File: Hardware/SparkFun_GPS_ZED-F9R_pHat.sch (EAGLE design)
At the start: 87 parts, among them J1 U.FL, J5 QWIIC_RIGHT_ANGLE, J6 RASPBERRYPI-40-PIN-GPIO_SMD_S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, U1 UBLOX_ZED_F9R, U2 HCPL-073L, U3 UHS_INVERTER_SCHMITT_TRIGGERS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, U4 UHS_INVERTER_SCHMITT_TRIGGERS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

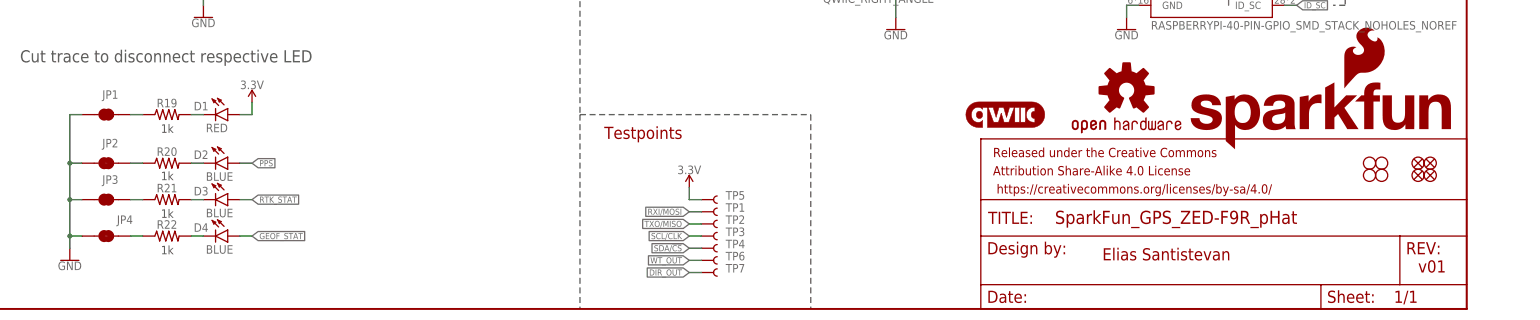
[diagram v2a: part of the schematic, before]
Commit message: Fixe RF trace, fixes silk, moves version number, fixes D+ and D- traces
* Changes jumper labels in schematic
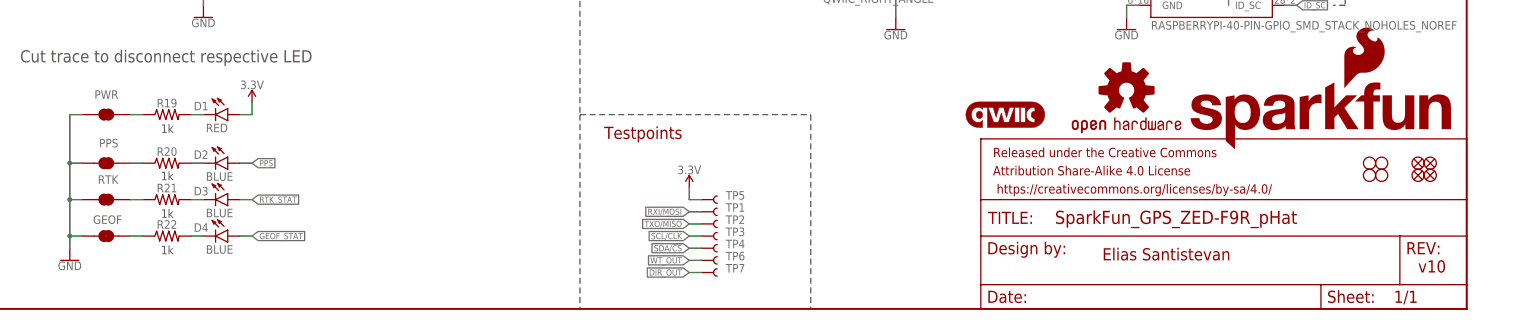
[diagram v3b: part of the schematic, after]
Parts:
- renumbered JP1 to PWR, JP2 to PPS, JP3 to RTK, JP4 to GEOF
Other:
- note added: "v10"
- note removed: "v01"
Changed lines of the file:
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@@
 <part name="R19" library="SparkFun-Resistors" deviceset="1KOHM" device="-0603-1/10W-1%" value="1k"/>
 <part name="SUPPLY7" library="SparkFun-PowerSymbols" deviceset="3.3V" device=""/>
-<part name="JP1" library="SparkFun-Jumpers" deviceset="JUMPER-SMT_2_NC_TRACE" device="_SILK" package3d_urn="urn:adsk.eagle:package:39281/1" value="JUMPER-SMT_2_NC_TRACE_SILK"/>
+<part name="PWR" library="SparkFun-Jumpers" deviceset="JUMPER-SMT_2_NC_TRACE" device="_SILK" package3d_urn="urn:adsk.eagle:package:39281/1" value="JUMPER-SMT_2_NC_TRACE_SILK"/>
 <part name="GND6" library="SparkFun-PowerSymbols" deviceset="GND" device=""/>
 <part name="GND7" library="SparkFun-PowerSymbols" deviceset="GND" device=""/>
@@
 <part name="R20" library="SparkFun-Resistors" deviceset="1KOHM" device="-0603-1/10W-1%" value="1k"/>
 <part name="R21" library="SparkFun-Resistors" deviceset="1KOHM" device="-0603-1/10W-1%" value="1k"/>
-<part name="JP3" library="SparkFun-Jumpers" deviceset="JUMPER-SMT_2_NC_TRACE" device="_SILK" package3d_urn="urn:adsk.eagle:package:39281/1" value="JUMPER-SMT_2_NC_TRACE_SILK"/>
-<part name="JP2" library="SparkFun-Jumpers" deviceset="JUMPER-SMT_2_NC_TRACE" device="_SILK" package3d_urn="urn:adsk.eagle:package:39281/1" value="JUMPER-SMT_2_NC_TRACE_SILK"/>
+<part name="RTK" library="SparkFun-Jumpers" deviceset="JUMPER-SMT_2_NC_TRACE" device="_SILK" package3d_urn="urn:adsk.eagle:package:39281/1" value="JUMPER-SMT_2_NC_TRACE_SILK"/>
+<part name="PPS" library="SparkFun-Jumpers" deviceset="JUMPER-SMT_2_NC_TRACE" device="_SILK" package3d_urn="urn:adsk.eagle:package:39281/1" value="JUMPER-SMT_2_NC_TRACE_SILK"/>
 <part name="GND19" library="SparkFun-PowerSymbols" deviceset="GND" device=""/>
 <part name="D2" library="SparkFun-LED" deviceset="LED-BLUE" device="0603" value="BLUE"/>
@@
 <part name="GND9" library="SparkFun-PowerSymbols" deviceset="GND" device=""/>
 <part name="R22" library="SparkFun-Resistors" deviceset="1KOHM" device="-0603-1/10W-1%" value="1k"/>
-<part name="JP4" library="SparkFun-Jumpers" deviceset="JUMPER-SMT_2_NC_TRACE" device="_SILK" package3d_urn="urn:adsk.eagle:package:39281/1" value="JUMPER-SMT_2_NC_TRACE_SILK"/>
+<part name="GEOF" library="SparkFun-Jumpers" deviceset="JUMPER-SMT_2_NC_TRACE" device="_SILK" package3d_urn="urn:adsk.eagle:package:39281/1" value="JUMPER-SMT_2_NC_TRACE_SILK"/>
 <part name="D4" library="SparkFun-LED" deviceset="LED-BLUE" device="0603" value="BLUE"/>
 <part name="FB1" library="SparkFun-Coils" deviceset="FERRITE_BEAD_GNSS" device="" value="120NH"/>
@@
 <sheet>
 <plain>
-<text x="421.64" y="7.62" size="2.54" layer="94" font="vector">v01</text>
+<text x="421.64" y="7.62" size="2.54" layer="94" font="vector">v10</text>
 <text x="355.6" y="10.16" size="2.54" layer="94" font="vector">Elias Santistevan</text>
 <text x="5.08" y="269.24" size="3.81" layer="94" font="vector">Dead Reckoning Module - ZED-F9R</text>
@@
 <attribute name="VALUE" x="177.8" y="45.974" size="1.778" layer="96" align="bottom-center"/>
 </instance>
-<instance part="JP1" gate="G$1" x="147.32" y="40.64" smashed="yes">
+<instance part="PWR" gate="G$1" x="147.32" y="40.64" smashed="yes">
 <attribute name="NAME" x="149.86" y="45.72" size="1.778" layer="95" font="vector" rot="R180"/>
 </instance>
@@
 <attribute name="NAME" x="160.02" y="24.384" size="1.778" layer="95" font="vector" align="bottom-center"/>
 </instance>
-<instance part="JP3" gate="G$1" x="147.32" y="22.86" smashed="yes">
+<instance part="RTK" gate="G$1" x="147.32" y="22.86" smashed="yes">
 <attribute name="NAME" x="149.86" y="27.94" size="1.778" layer="95" font="vector" rot="R180"/>
 </instance>
-<instance part="JP2" gate="G$1" x="147.32" y="30.48" smashed="yes">
+<instance part="PPS" gate="G$1" x="147.32" y="30.48" smashed="yes">
 <attribute name="NAME" x="149.86" y="35.56" size="1.778" layer="95" font="vector" rot="R180"/>
 </instance>
@@
 <attribute name="NAME" x="160.02" y="16.764" size="1.778" layer="95" font="vector" align="bottom-center"/>
 </instance>
-<instance part="JP4" gate="G$1" x="147.32" y="15.24" smashed="yes">
-<attribute name="NAME" x="152.908" y="19.558" size="1.778" layer="95" font="vector" rot="R180"/>
+<instance part="GEOF" gate="G$1" x="147.32" y="15.24" smashed="yes">
+<attribute name="NAME" x="150.622" y="19.558" size="1.778" layer="95" font="vector" rot="R180"/>
 </instance>
 <instance part="D4" gate="G$1" x="172.72" y="15.24" smashed="yes" rot="R270">
@@
 </segment>
 <segment>
-<pinref part="JP3" gate="G$1" pin="1"/>
+<pinref part="RTK" gate="G$1" pin="1"/>
 <wire x1="142.24" y1="22.86" x2="139.7" y2="22.86" width="0.1524" layer="91"/>
 <wire x1="139.7" y1="22.86" x2="139.7" y2="15.24" width="0.1524" layer="91"/>
 <pinref part="GND19" gate="1" pin="GND"/>
-<pinref part="JP2" gate="G$1" pin="1"/>
+<pinref part="PPS" gate="G$1" pin="1"/>
 <wire x1="139.7" y1="15.24" x2="139.7" y2="12.7" width="0.1524" layer="91"/>
 <wire x1="142.24" y1="30.48" x2="139.7" y2="30.48" width="0.1524" layer="91"/>
 <wire x1="139.7" y1="30.48" x2="139.7" y2="22.86" width="0.1524" layer="91"/>
 <junction x="139.7" y="22.86"/>
-<pinref part="JP1" gate="G$1" pin="1"/>
+<pinref part="PWR" gate="G$1" pin="1"/>
 <wire x1="142.24" y1="40.64" x2="139.7" y2="40.64" width="0.1524" layer="91"/>
 <wire x1="139.7" y1="40.64" x2="139.7" y2="30.48" width="0.1524" layer="91"/>
 <junction x="139.7" y="30.48"/>
-<pinref part="JP4" gate="G$1" pin="1"/>
+<pinref part="GEOF" gate="G$1" pin="1"/>
 <wire x1="142.24" y1="15.24" x2="139.7" y2="15.24" width="0.1524" layer="91"/>
 <junction x="139.7" y="15.24"/>
@@
 <net name="N$22" class="0">
 <segment>
-<pinref part="JP3" gate="G$1" pin="2"/>
+<pinref part="RTK" gate="G$1" pin="2"/>
 <pinref part="R21" gate="G$1" pin="1"/>
 <wire x1="152.4" y1="22.86" x2="154.94" y2="22.86" width="0.1524" layer="91"/>
@@
 <net name="N$23" class="0">
 <segment>
-<pinref part="JP2" gate="G$1" pin="2"/>
+<pinref part="PPS" gate="G$1" pin="2"/>
 <pinref part="R20" gate="G$1" pin="1"/>
 <wire x1="152.4" y1="30.48" x2="154.94" y2="30.48" width="0.1524" layer="91"/>
@@
 <segment>
 <pinref part="R19" gate="G$1" pin="1"/>
-<pinref part="JP1" gate="G$1" pin="2"/>
+<pinref part="PWR" gate="G$1" pin="2"/>
 <wire x1="154.94" y1="40.64" x2="152.4" y2="40.64" width="0.1524" layer="91"/>
 </segment>
@@
 <net name="N$16" class="0">
 <segment>
-<pinref part="JP4" gate="G$1" pin="2"/>
+<pinref part="GEOF" gate="G$1" pin="2"/>
 <pinref part="R22" gate="G$1" pin="1"/>
 <wire x1="152.4" y1="15.24" x2="154.94" y2="15.24" width="0.1524" layer="91"/>

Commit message: Updates silk, fixes RF trace, moves some traces for better clearance, adds wt/dir text to schematic
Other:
- note added: "Wheel Tick/Direction Input: 3-24V"
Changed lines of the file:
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@@
 <wire x1="160.02" y1="213.36" x2="297.18" y2="213.36" width="0.1524" layer="97" style="shortdash"/>
 <wire x1="86.36" y1="134.62" x2="86.36" y2="0" width="0.1524" layer="97" style="shortdash"/>
+<text x="299.72" y="175.26" size="1.778" layer="97" font="vector">Wheel Tick/Direction
+Input: 3-24V</text>
 </plain>
 <instances>

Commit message: Adds 33 Ohm resistor arrays and custom silk
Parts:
- removed R25: 5.1k, SparkFun-Resistors:5.1KOHM-0402-1/16W-1%
- removed R26, R29, R30: 3.3k, SparkFun-Resistors:3.3KOHM-0603-1/10W-1%
- removed R27, R28: 27, SparkFun-Resistors:27OHM-0603-1/10W-1%
- removed R31, R32: 910, classified:910OHM-0603-1/10W-5%
- removed R33, R34: 470, SparkFun-Resistors:470OHM-0603-1/10W-1%
- R10, R11, R12, R9: value 33 -> 1k; device SparkFun-Resistors:33OHM-0603-1/10W-1% -> SparkFun-Resistors:1KOHM-0603-1/10W-1%
- R13, R8: value 33 -> 2.2k; device SparkFun-Resistors:33OHM-0603-1/10W-1% -> SparkFun-Resistors:2.2KOHM-0603-1/10W-1%
- R14, R15: value 33 -> 5.1k; device SparkFun-Resistors:33OHM-0603-1/10W-1% -> SparkFun-Resistors:5.1KOHM-0402-1/16W-1%
- R16: value 33 -> 3.3k; device SparkFun-Resistors:33OHM-0603-1/10W-1% -> SparkFun-Resistors:3.3KOHM-0603-1/10W-1%
- R17: value 33 -> 27; device SparkFun-Resistors:33OHM-0603-1/10W-1% -> SparkFun-Resistors:27OHM-0603-1/10W-1%
- R18: value 2.2k -> 27; device SparkFun-Resistors:2.2KOHM-0603-1/10W-1% -> SparkFun-Resistors:27OHM-0603-1/10W-1%
- R19, R20: value 1k -> 3.3k; device SparkFun-Resistors:1KOHM-0603-1/10W-1% -> SparkFun-Resistors:3.3KOHM-0603-1/10W-1%
- R21, R22: value 1k -> 910; device SparkFun-Resistors:1KOHM-0603-1/10W-1% -> classified:910OHM-0603-1/10W-5%
- R23: value 2.2k -> 470; device SparkFun-Resistors:2.2KOHM-0603-1/10W-1% -> SparkFun-Resistors:470OHM-0603-1/10W-1%
- R24: value 5.1k -> 470; device SparkFun-Resistors:5.1KOHM-0402-1/16W-1% -> SparkFun-Resistors:470OHM-0603-1/10W-1%
- R3, R5, R6, R7: device SparkFun-Resistors:33OHM-0603-1/10W-1% -> SparkFun-Resistors:33OHM_RESISTOR_ARRAY
- renumbered GEOF to JP4, PPS to JP2, PWR to JP1, RTK to JP3
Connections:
- net !RESET: now also R3A.1; no longer R5.2
- net !SAFEBOOT: now also R3B.1; no longer R17.2
- net 3.3V: now also R21.2, R22.2; no longer R31.2, R32.2
- net DIR+: now also R20.1; no longer R30.1
- net DIR_IN: now also R23.2; no longer R33.2
- net DIR_OUT: now also R6C.2; no longer R4.1
- net DIR_SCHMITT: now also R22.1; no longer R32.1
- net DMINUS: now also R18.2; no longer R28.2
- net DPLUS: now also R17.2; no longer R27.2
- net GEOF_STAT: now also R7B.2; no longer R14.2
- net GND: now also R14.1, R15.1; no longer R24.1, R25.1
- net INT: now also R3C.1; no longer R6.2
- net N$1: now also R13.2; no longer R23.2
- net N$12: now also R14.2; no longer R24.2
- net N$13: now also R3A.2; no longer R5.1
- net N$14: now also R3C.2; no longer R6.1
- net N$15: now also R5C.2; no longer R7.1
- net N$16: now also R12.1; no longer R22.1
- net N$17: now also R12.2; no longer R22.2
- net N$18: now also R15.2; no longer R25.2
- net N$19: now also R5D.2; no longer R8.1
- net N$2: now also R16.2; no longer R26.2
- net N$20: now also R4.1; no longer R9.1
- net N$21: now also R5A.2; no longer R10.1
- net N$22: now also R11.1; no longer R21.1
- net N$23: now also R10.1; no longer R20.1
- net N$24: now also R10.2; no longer R20.2
- net N$25: now also R11.2; no longer R21.2
- net N$26: now also R5B.2; no longer R11.1
- net N$27: now also R19.2, R24.1; no longer R29.2, R34.1
- net N$28: now also R7B.1; no longer R14.1
- net N$29: now also R7A.1; no longer R15.1
- net N$3: now also R8.2; no longer R18.2
- net N$30: now also R3D.2; no longer R16.1
- net N$31: now also R3B.2; no longer R17.1
- net N$32: now also R6A.1; no longer R12.1
- net N$33: now also R6B.1; no longer R13.1
- net N$34: now also R6D.1; no longer R3.2
- net N$35: now also R6C.1; no longer R4.2
- net N$36: now also R20.2, R23.1; no longer R30.2, R33.1
- net N$4: now also R9.2; no longer R19.2
- net N$6: now also R18.1; no longer R28.1
- net N$7: now also R17.1; no longer R27.1
- net N$8: now also R9.1; no longer R19.1
- net PPS: now also R3D.1; no longer R16.2
- net QWIIC_SCL: now also R8.1; no longer R18.1
- net QWIIC_SDA: now also R13.1; no longer R23.1
- net RTK_STAT: now also R7A.2; no longer R15.2
- net RXI/MOSI: now also R5B.1; no longer R11.2
- net RXI2: now also R6B.2; no longer R13.2
- net SCL/CLK: now also R5D.1; no longer R8.2
- net SDA/!CS: now also R5C.1; no longer R7.2
- net TXO/MISO: now also R5A.1; no longer R10.2
- net TXO2: now also R6A.2; no longer R12.2
- net TX_READY: now also R4.2; no longer R9.2
- net V_BATT: now also R16.1; no longer R26.1
- net WT+: now also R19.1; no longer R29.1
- net WT_IN: now also R24.2; no longer R34.2
- net WT_OUT: now also R6D.2; no longer R3.1
- net WT_SCHMITT: now also R21.1; no longer R31.1
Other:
- moved on the sheet: R10, R11, R12, R13, R16, R17, R18, R19, R20, R21, R22, R23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

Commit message: Updates all parts to parts in the Eagle Library
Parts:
- D7, D8: value 0.5A/40V/420mV -> 15V; device classified:BZX84_DIODE -> SparkFun-DiscreteSemi:DIODE-ZENER-BZX84C15LT3G
- R3, R5, R6, R7: device SparkFun-Resistors:33OHM_RESISTOR_ARRAY -> SparkFun-Resistors:33OHM_RA-1206-1/16W-5%
- U1: value UBLOX_ZED_F9R -> U-BLOX_ZED_F9R; device classified:UBLOX_ZED_F9R -> SparkFun-GPS:U-BLOX_ZED_F9R
- U2: value HCPL-073L -> DUAL-OPTO_HCPL-073L; device classified:HCPL-073L -> SparkFun-DiscreteSemi:DUAL-OPTO_HCPL-073L
- U3, U4: device classified:UHS_INVERTER_SCHMITT_TRIGGERSIP6 -> SparkFun-IC-Amplifiers:UHS_INVERTER_SCHMITT_TRIGGERSIP6
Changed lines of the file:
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@@
 <part name="GND7" library="SparkFun-PowerSymbols" deviceset="GND" device=""/>
 <part name="BT1" library="SparkFun-Batteries" deviceset="ML414H_IV01E_BATTERY" device=""/>
-<part name="U1" library="classified" deviceset="UBLOX_ZED_F9R" device=""/>
+<part name="U1" library="SparkFun-GPS" deviceset="U-BLOX_ZED_F9R" device=""/>
 <part name="FRAME1" library="SparkFun-Aesthetics" deviceset="FRAME-LEDGER" device=""/>
 <part name="C3" library="SparkFun-Capacitors" deviceset="47PF" device="-0402-25V-5%-X7R" value="47pF"/>
@@
 <part name="C5" library="SparkFun-Capacitors" deviceset="1.0NF/1000PF" device="-0402-25V-10%-X7R" value="1nF"/>
 <part name="C6" library="SparkFun-Capacitors" deviceset="1.0NF/1000PF" device="-0402-25V-10%-X7R" value="1nF"/>
-<part name="D8" library="classified" deviceset="BZX84_DIODE" device="" value="0.5A/40V/420mV"/>
+<part name="D8" library="SparkFun-DiscreteSemi" deviceset="DIODE-ZENER" device="-BZX84C15LT3G" value="15V"/>
 <part name="R21" library="classified" deviceset="910OHM-0603-1/10W-5%" device="" value="910"/>
 <part name="R22" library="classified" deviceset="910OHM-0603-1/10W-5%" device="" value="910"/>
-<part name="U2" library="classified" deviceset="HCPL-073L" device=""/>
+<part name="U2" library="SparkFun-DiscreteSemi" deviceset="DUAL-OPTO_HCPL-073L" device=""/>
 <part name="C4" library="SparkFun-Capacitors" deviceset="0.1UF" device="-0402-6.3V-10%-X7R" value="0.1uF"/>
 <part name="SUPPLY9" library="SparkFun-PowerSymbols" deviceset="3.3V" device=""/>
 <part name="GND11" library="SparkFun-PowerSymbols" deviceset="GND" device=""/>
-<part name="U3" library="classified" deviceset="UHS_INVERTER_SCHMITT_TRIGGER" device="SIP6" value="UHS_INVERTER_SCHMITT_TRIGGERSIP6"/>
-<part name="U4" library="classified" deviceset="UHS_INVERTER_SCHMITT_TRIGGER" device="SIP6" value="UHS_INVERTER_SCHMITT_TRIGGERSIP6"/>
+<part name="U3" library="SparkFun-IC-Amplifiers" deviceset="UHS_INVERTER_SCHMITT_TRIGGER" device="SIP6" value="UHS_INVERTER_SCHMITT_TRIGGERSIP6"/>
+<part name="U4" library="SparkFun-IC-Amplifiers" deviceset="UHS_INVERTER_SCHMITT_TRIGGER" device="SIP6" value="UHS_INVERTER_SCHMITT_TRIGGERSIP6"/>
 <part name="SUPPLY10" library="SparkFun-PowerSymbols" deviceset="3.3V" device=""/>
 <part name="GND12" library="SparkFun-PowerSymbols" deviceset="GND" device=""/>
-<part name="D7" library="classified" deviceset="BZX84_DIODE" device="" value="0.5A/40V/420mV"/>
+<part name="D7" library="SparkFun-DiscreteSemi" deviceset="DIODE-ZENER" device="-BZX84C15LT3G" value="15V"/>
 <part name="SUPPLY12" library="SparkFun-PowerSymbols" deviceset="3.3V" device=""/>
 <part name="SUPPLY13" library="SparkFun-PowerSymbols" deviceset="3.3V" device=""/>
@@
 <part name="GND24" library="SparkFun-PowerSymbols" deviceset="GND" device=""/>
 <part name="J4" library="SparkFun-Connectors" deviceset="CONN_08" device="NO_SILK_FEMALE_PTH"/>
-<part name="R3" library="SparkFun-Resistors" deviceset="33OHM_RESISTOR_ARRAY" device="" value="33"/>
-<part name="R5" library="SparkFun-Resistors" deviceset="33OHM_RESISTOR_ARRAY" device="" value="33"/>
-<part name="R6" library="SparkFun-Resistors" deviceset="33OHM_RESISTOR_ARRAY" device="" value="33"/>
-<part name="R7" library="SparkFun-Resistors" deviceset="33OHM_RESISTOR_ARRAY" device="" value="33"/>
+<part name="R3" library="SparkFun-Resistors" deviceset="33OHM_RA" device="-1206-1/16W-5%" value="33"/>
+<part name="R5" library="SparkFun-Resistors" deviceset="33OHM_RA" device="-1206-1/16W-5%" value="33"/>
+<part name="R6" library="SparkFun-Resistors" deviceset="33OHM_RA" device="-1206-1/16W-5%" value="33"/>
+<part name="R7" library="SparkFun-Resistors" deviceset="33OHM_RA" device="-1206-1/16W-5%" value="33"/>
 </parts>
 <sheets>
@@
 <instance part="U2" gate="G$1" x="325.12" y="226.06" smashed="yes">
 <attribute name="NAME" x="317.5" y="236.982" size="1.778" layer="95"/>
-<attribute name="VALUE" x="317.5" y="210.82" size="1.778" layer="95"/>
+<attribute name="VALUE" x="312.674" y="205.486" size="1.778" layer="95"/>
 </instance>
 <instance part="C4" gate="G$1" x="312.42" y="226.06" smashed="yes">

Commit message: Replaces 910 Ohm resistor with part from Eagle Library
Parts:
- R21, R22: device classified:910OHM-0603-1/10W-5% -> SparkFun-Resistors:910OHM-0603-1/10W-5%
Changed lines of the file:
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@@
 <part name="C6" library="SparkFun-Capacitors" deviceset="1.0NF/1000PF" device="-0402-25V-10%-X7R" value="1nF"/>
 <part name="D8" library="SparkFun-DiscreteSemi" deviceset="DIODE-ZENER" device="-BZX84C15LT3G" value="15V"/>
-<part name="R21" library="classified" deviceset="910OHM-0603-1/10W-5%" device="" value="910"/>
-<part name="R22" library="classified" deviceset="910OHM-0603-1/10W-5%" device="" value="910"/>
+<part name="R21" library="SparkFun-Resistors" deviceset="910OHM" device="-0603-1/10W-5%" value="910"/>
+<part name="R22" library="SparkFun-Resistors" deviceset="910OHM" device="-0603-1/10W-5%" value="910"/>
 <part name="U2" library="SparkFun-DiscreteSemi" deviceset="DUAL-OPTO_HCPL-073L" device=""/>
 <part name="C4" library="SparkFun-Capacitors" deviceset="0.1UF" device="-0402-6.3V-10%-X7R" value="0.1uF"/>
